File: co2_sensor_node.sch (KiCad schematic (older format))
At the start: 0 parts

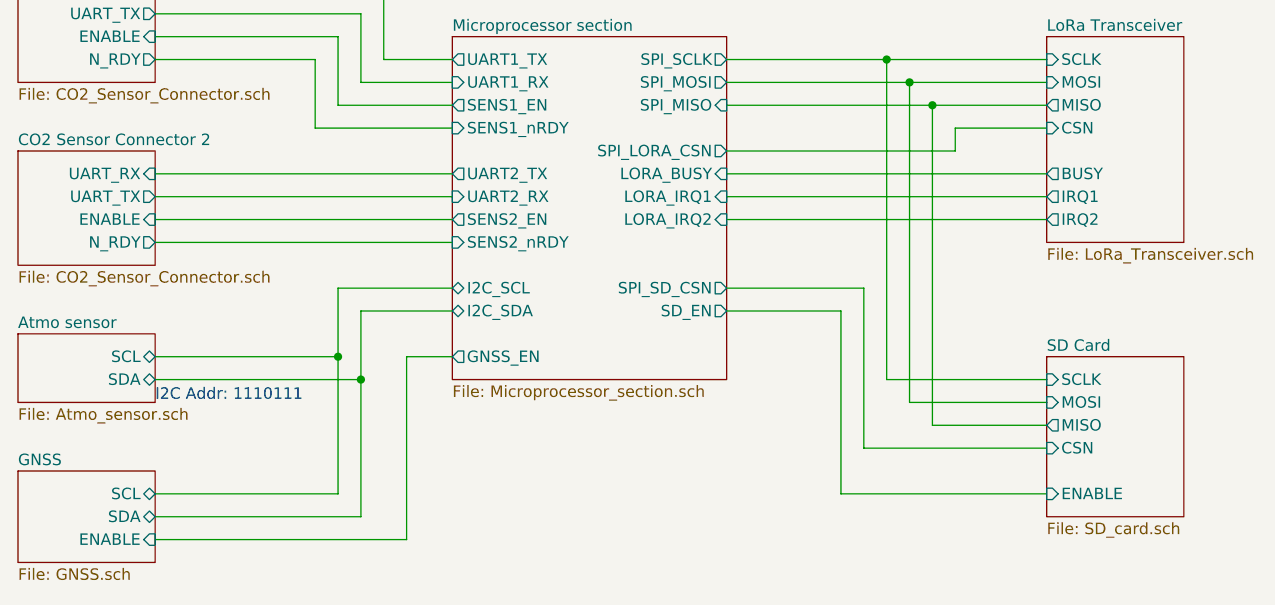
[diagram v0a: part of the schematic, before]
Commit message: Change BME280 out for connector
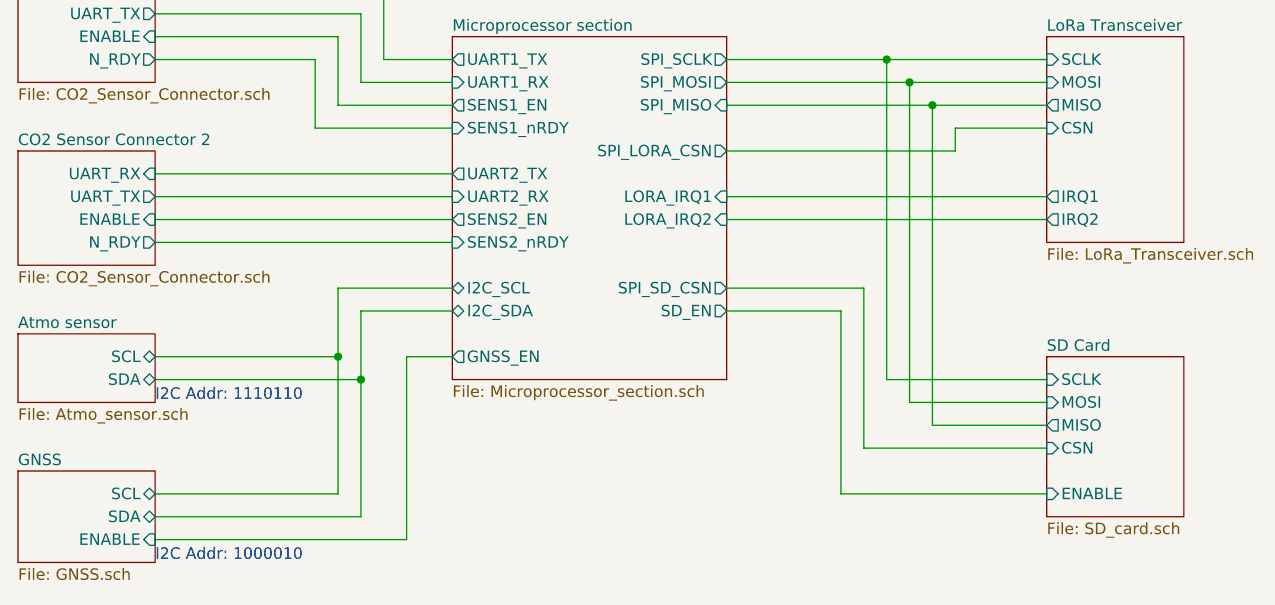
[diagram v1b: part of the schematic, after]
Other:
- note added: "I2C Addr: 1000010"
- note added: "I2C Addr: 1110110"
- note removed: "I2C Addr: 1110111"
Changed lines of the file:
@@
 F4 "MISO" O L 7500 3300 50
 F5 "CSN" I L 7500 3400 50
-F6 "BUSY" O L 7500 3600 50
-F7 "IRQ1" O L 7500 3700 50
-F8 "IRQ2" O L 7500 3800 50
+F6 "IRQ1" O L 7500 3700 50
+F7 "IRQ2" O L 7500 3800 50
 $EndSheet
 Wire Wire Line
@@
 	6800 4500 7500 4500
 Wire Wire Line
-	6100 3600 7500 3600
-Wire Wire Line
 	6100 3700 7500 3700
 Wire Wire Line
@@
 F15 "SENS2_EN" O L 4900 3800 50
 F16 "SENS2_nRDY" I L 4900 3900 50
-F17 "LORA_BUSY" I R 6100 3600 50
-F18 "LORA_IRQ1" I R 6100 3700 50
-F19 "LORA_IRQ2" I R 6100 3800 50
-F20 "GNSS_EN" O L 4900 4400 50
-F21 "SD_EN" O R 6100 4200 50
+F17 "LORA_IRQ1" I R 6100 3700 50
+F18 "LORA_IRQ2" I R 6100 3800 50
+F19 "GNSS_EN" O L 4900 4400 50
+F20 "SD_EN" O R 6100 4200 50
 $EndSheet
 Wire Wire Line
@@
 Wire Wire Line
 	3600 3600 4900 3600
+Text Notes 3600 5300 0    50   ~ 0
+I2C Addr: 1000010
 Text Notes 3600 4600 0    50   ~ 0
-I2C Addr: 1110111
+I2C Addr: 1110110
 $EndSCHEMATC

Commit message: Start PCB layout
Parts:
- added H1, H2, H3, H4: MountingHole, MountingHole:MountingHole_3.2mm_M3, symbol Mechanical:MountingHole
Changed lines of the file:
@@
 Text Notes 3600 4600 0    50   ~ 0
 I2C Addr: 1110110
+$Comp
+L Mechanical:MountingHole H1
+U 1 1 60AFB8C6
+P 9500 5000
+F 0 "H1" H 9600 5046 50  0000 L CNN
+F 1 "MountingHole" H 9600 4955 50  0000 L CNN
+F 2 "MountingHole:MountingHole_3.2mm_M3" H 9500 5000 50  0001 C CNN
+F 3 "~" H 9500 5000 50  0001 C CNN
+	1    9500 5000
+	1    0    0    -1
+$EndComp
+$Comp
+L Mechanical:MountingHole H2
+U 1 1 60AFC708
+P 9500 5200
+F 0 "H2" H 9600 5246 50  0000 L CNN
+F 1 "MountingHole" H 9600 5155 50  0000 L CNN
+F 2 "MountingHole:MountingHole_3.2mm_M3" H 9500 5200 50  0001 C CNN
+F 3 "~" H 9500 5200 50  0001 C CNN
+	1    9500 5200
+	1    0    0    -1
+$EndComp
+$Comp
+L Mechanical:MountingHole H3
+U 1 1 60AFC7FA
+P 9500 5400
+F 0 "H3" H 9600 5446 50  0000 L CNN
+F 1 "MountingHole" H 9600 5355 50  0000 L CNN
+F 2 "MountingHole:MountingHole_3.2mm_M3" H 9500 5400 50  0001 C CNN
+F 3 "~" H 9500 5400 50  0001 C CNN
+	1    9500 5400
+	1    0    0    -1
+$EndComp
+$Comp
+L Mechanical:MountingHole H4
+U 1 1 60AFC8FD
+P 9500 5600
+F 0 "H4" H 9600 5646 50  0000 L CNN
+F 1 "MountingHole" H 9600 5555 50  0000 L CNN
+F 2 "MountingHole:MountingHole_3.2mm_M3" H 9500 5600 50  0001 C CNN
+F 3 "~" H 9500 5600 50  0001 C CNN
+	1    9500 5600
+	1    0    0    -1
+$EndComp
 $EndSCHEMATC

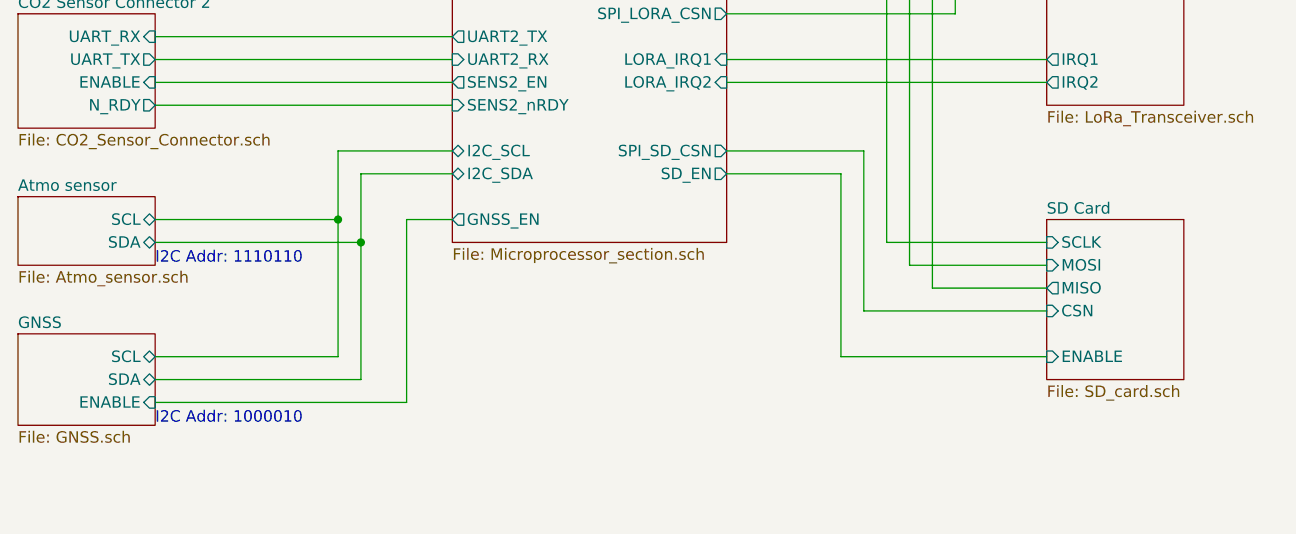
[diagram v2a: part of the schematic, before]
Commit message: Start changing design for long term chambers
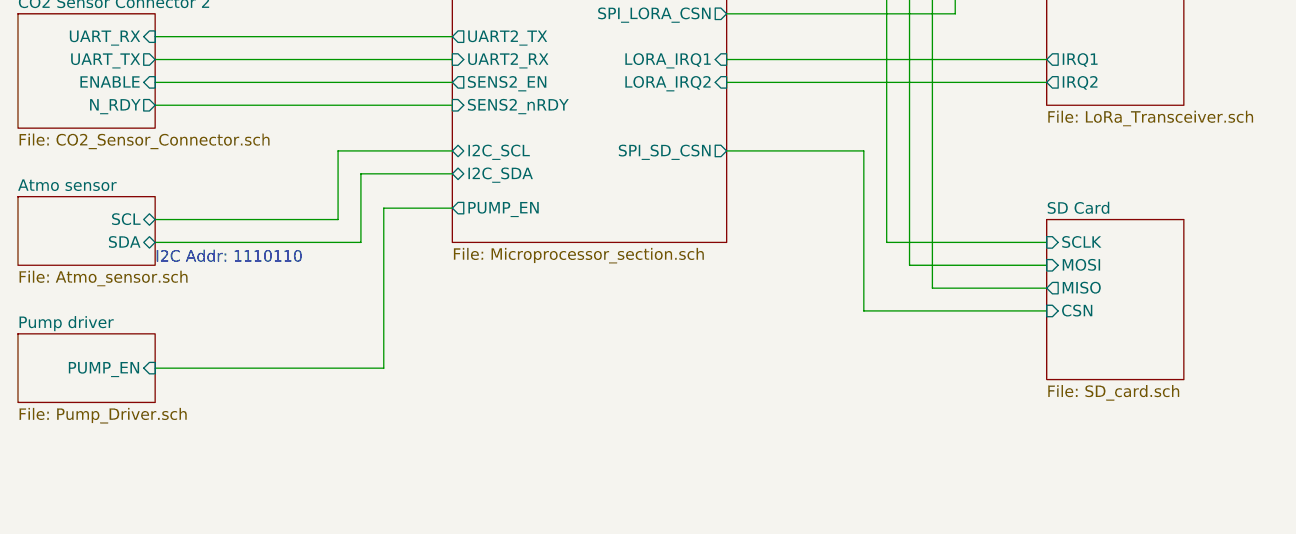
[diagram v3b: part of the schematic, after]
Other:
- note removed: "I2C Addr: 1000010"
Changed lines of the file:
@@
 F4 "MISO" O L 7500 4700 50
 F5 "CSN" I L 7500 4800 50
-F6 "ENABLE" I L 7500 5000 50
 $EndSheet
 $Sheet
@@
 	6100 3300 7000 3300
 Connection ~ 7000 3300
-$Sheet
-S 3000 4900 600  400
-U 60A8B3C8
-F0 "GNSS" 50
-F1 "GNSS.sch" 50
-F2 "SCL" B R 3600 5000 50
-F3 "SDA" B R 3600 5100 50
-F4 "ENABLE" I R 3600 5200 50
-$EndSheet
-Wire Wire Line
-	4400 4400 4400 5000
-Wire Wire Line
-	4400 5000 3600 5000
-Connection ~ 4400 4400
-Wire Wire Line
-	4500 4500 4500 5100
-Wire Wire Line
-	4500 5100 3600 5100
-Connection ~ 4500 4500
-Wire Wire Line
-	4900 4400 4700 4400
-Wire Wire Line
-	4700 4400 4700 5200
-Wire Wire Line
-	4700 5200 3600 5200
 Wire Wire Line
 	7100 3400 7500 3400
@@
 Wire Wire Line
 	7000 3300 7500 3300
-Wire Wire Line
-	6100 4200 6600 4200
-Wire Wire Line
-	6600 4200 6600 5000
-Wire Wire Line
-	6600 5000 7500 5000
 $Sheet
 S 3000 1700 500  500
@@
 F17 "LORA_IRQ1" I R 6100 3700 50
 F18 "LORA_IRQ2" I R 6100 3800 50
-F19 "GNSS_EN" O L 4900 4400 50
-F20 "SD_EN" O R 6100 4200 50
+F19 "PUMP_EN" O L 4900 4350 50
 $EndSheet
 Wire Wire Line
@@
 Wire Wire Line
 	3600 3600 4900 3600
-Text Notes 3600 5300 0    50   ~ 0
-I2C Addr: 1000010
 Text Notes 3600 4600 0    50   ~ 0
 I2C Addr: 1110110
@@
 	1    0    0    -1
 $EndComp
+$Sheet
+S 3000 4900 600  300
+U 60BD38F8
+F0 "Pump driver" 50
+F1 "Pump_Driver.sch" 50
+F2 "PUMP_EN" I R 3600 5050 50
+$EndSheet
+Wire Wire Line
+	4900 4350 4600 4350
+Wire Wire Line
+	4600 5050 3600 5050
+Wire Wire Line
+	4600 4350 4600 5050
 $EndSCHEMATC

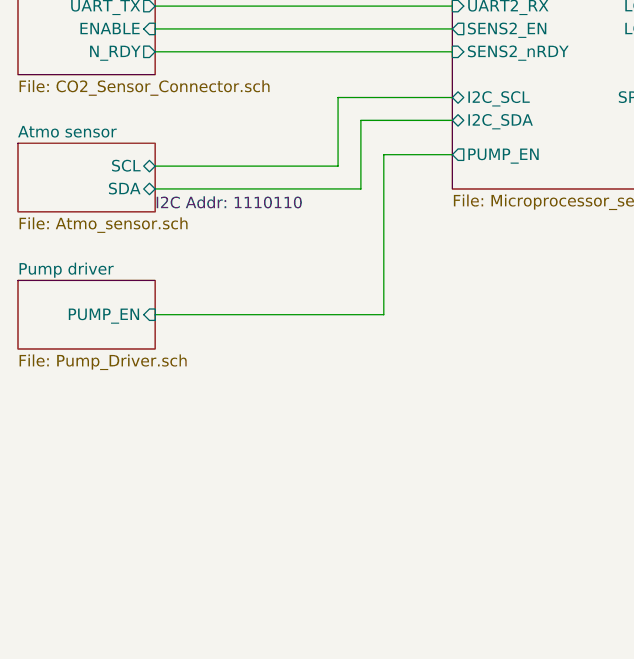
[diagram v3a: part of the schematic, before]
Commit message: Add connector for external chamber connection and change SMA to U.FL connector
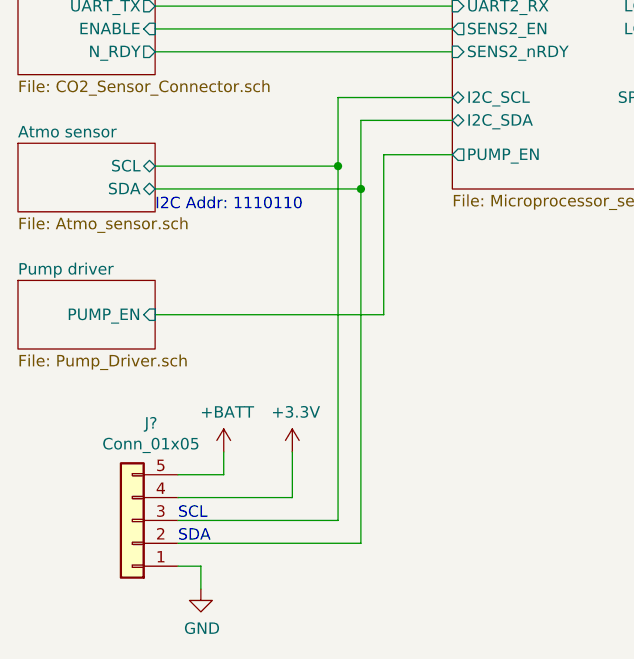
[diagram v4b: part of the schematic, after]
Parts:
- added J?: Conn_01x05, Connector_JST:JST_XH_B5B-XH-AM_1x05_P2.50mm_Vertical, symbol Connector_Generic:Conn_01x05
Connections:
- net Atmo sensor/SCL: now also J?.3 (Pin_3)
- net Atmo sensor/SDA: now also J?.2 (Pin_2)
- new net +3V3: J?.4 (Pin_4)
- new net +BATT: J?.5 (Pin_5)
- new net GND: J?.1 (Pin_1)
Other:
- note added: "SCL"
- note added: "SDA"
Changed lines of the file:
@@
 Wire Wire Line
 	4600 4350 4600 5050
+$Comp
+L Connector_Generic:Conn_01x05 J?
+U 1 1 6107D17A
+P 3500 5950
+F 0 "J?" H 3418 5525 50  0000 C CNN
+F 1 "Conn_01x05" H 3418 5616 50  0000 C CNN
+F 2 "Connector_JST:JST_XH_B5B-XH-AM_1x05_P2.50mm_Vertical" H 3418 5617 50  0001 C CNN
+F 3 "~" H 3500 5950 50  0001 C CNN
+	1    3500 5950
+	-1   0    0    1
+$EndComp
+$Comp
+L power:+BATT #PWR?
+U 1 1 6107E2E0
+P 3900 5650
+F 0 "#PWR?" H 3900 5500 50  0001 C CNN
+F 1 "+BATT" H 3915 5823 50  0000 C CNN
+F 2 "" H 3900 5650 50  0001 C CNN
+F 3 "" H 3900 5650 50  0001 C CNN
+	1    3900 5650
+	1    0    0    -1
+$EndComp
+$Comp
+L power:+3.3V #PWR?
+U 1 1 6107E8D3
+P 4200 5650
+F 0 "#PWR?" H 4200 5500 50  0001 C CNN
+F 1 "+3.3V" H 4215 5823 50  0000 C CNN
+F 2 "" H 4200 5650 50  0001 C CNN
+F 3 "" H 4200 5650 50  0001 C CNN
+	1    4200 5650
+	1    0    0    -1
+$EndComp
+$Comp
+L power:GND #PWR?
+U 1 1 6107ECD8
+P 3800 6250
+F 0 "#PWR?" H 3800 6000 50  0001 C CNN
+F 1 "GND" H 3805 6077 50  0000 C CNN
+F 2 "" H 3800 6250 50  0001 C CNN
+F 3 "" H 3800 6250 50  0001 C CNN
+	1    3800 6250
+	1    0    0    -1
+$EndComp
+Wire Wire Line
+	3700 6150 3800 6150
+Wire Wire Line
+	3800 6150 3800 6250
+Wire Wire Line
+	3700 5750 3900 5750
+Wire Wire Line
+	3900 5750 3900 5650
+Wire Wire Line
+	3700 5850 4200 5850
+Wire Wire Line
+	4200 5850 4200 5650
+Wire Wire Line
+	4400 4400 4400 5950
+Wire Wire Line
+	4400 5950 3700 5950
+Connection ~ 4400 4400
+Wire Wire Line
+	4500 4500 4500 6050
+Wire Wire Line
+	4500 6050 3700 6050
+Connection ~ 4500 4500
+Text Notes 3700 5950 0    50   ~ 0
+SCL
+Text Notes 3700 6050 0    50   ~ 0
+SDA
 $EndSCHEMATC

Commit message: Finalize schematic
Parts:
- removed J?: Conn_01x05, Connector_JST:JST_XH_B5B-XH-AM_1x05_P2.50mm_Vertical, symbol Connector_Generic:Conn_01x05
- added J?: Conn_01x04, Connector_JST:JST_XH_S4B-XH-A_1x04_P2.50mm_Horizontal, symbol Connector_Generic:Conn_01x04
- added J?: Conn_01x06, Connector_JST:JST_XH_S6B-XH-A_1x06_P2.50mm_Horizontal, symbol Connector_Generic:Conn_01x06
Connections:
- net +3V3: now also J?.1 (Pin_1), J?.2 (Pin_2)
- net +BATT: now also J?.1 (Pin_1)
- net Atmo sensor/SCL: now also J?.3 (Pin_3)
- net Atmo sensor/SDA: now also J?.4 (Pin_4)
- net GND: now also J?.3 (Pin_3), J?.4 (Pin_4), J?.5 (Pin_5), J?.6 (Pin_6)
- new net Microprocessor section/TEMPSENSOR: J?.2 (Pin_2)
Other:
- note added: "Header for\nexternal chamber"
- note added: "Temp header for use with DS18B20 sensor\n"
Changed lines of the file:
@@
 F18 "LORA_IRQ2" I R 6100 3800 50
 F19 "PUMP_EN" O L 4900 4350 50
+F20 "TEMPSENSOR" I R 6100 4350 50
 $EndSheet
 Wire Wire Line
@@
 	4600 4350 4600 5050
 $Comp
-L Connector_Generic:Conn_01x05 J?
-U 1 1 6107D17A
-P 3500 5950
-F 0 "J?" H 3418 5525 50  0000 C CNN
-F 1 "Conn_01x05" H 3418 5616 50  0000 C CNN
-F 2 "Connector_JST:JST_XH_B5B-XH-AM_1x05_P2.50mm_Vertical" H 3418 5617 50  0001 C CNN
-F 3 "~" H 3500 5950 50  0001 C CNN
-	1    3500 5950
-	-1   0    0    1
-$EndComp
-$Comp
-L power:+BATT #PWR?
+L power:+BATT #PWR08
 U 1 1 6107E2E0
 P 3900 5650
-F 0 "#PWR?" H 3900 5500 50  0001 C CNN
+F 0 "#PWR08" H 3900 5500 50  0001 C CNN
 F 1 "+BATT" H 3915 5823 50  0000 C CNN
 F 2 "" H 3900 5650 50  0001 C CNN
@@
 $EndComp
 $Comp
-L power:+3.3V #PWR?
+L power:+3.3V #PWR042
 U 1 1 6107E8D3
 P 4200 5650
-F 0 "#PWR?" H 4200 5500 50  0001 C CNN
+F 0 "#PWR042" H 4200 5500 50  0001 C CNN
 F 1 "+3.3V" H 4215 5823 50  0000 C CNN
 F 2 "" H 4200 5650 50  0001 C CNN
@@
 $EndComp
 $Comp
-L power:GND #PWR?
+L power:GND #PWR03
 U 1 1 6107ECD8
-P 3800 6250
-F 0 "#PWR?" H 3800 6000 50  0001 C CNN
-F 1 "GND" H 3805 6077 50  0000 C CNN
-F 2 "" H 3800 6250 50  0001 C CNN
-F 3 "" H 3800 6250 50  0001 C CNN
-	1    3800 6250
+P 3800 6350
+F 0 "#PWR03" H 3800 6100 50  0001 C CNN
+F 1 "GND" H 3805 6177 50  0000 C CNN
+F 2 "" H 3800 6350 50  0001 C CNN
+F 3 "" H 3800 6350 50  0001 C CNN
+	1    3800 6350
 	1    0    0    -1
 $EndComp
@@
 Wire Wire Line
 	4400 5950 3700 5950
-Connection ~ 4400 4400
 Wire Wire Line
 	4500 4500 4500 6050
 Wire Wire Line
 	4500 6050 3700 6050
-Connection ~ 4500 4500
 Text Notes 3700 5950 0    50   ~ 0
 SCL
 Text Notes 3700 6050 0    50   ~ 0
 SDA
+Connection ~ 4400 4400
+Connection ~ 4500 4500
+$Comp
+L power:+3.3V #PWR043
+U 1 1 60D3DB8F
+P 6500 5150
+F 0 "#PWR043" H 6500 5000 50  0001 C CNN
+F 1 "+3.3V" H 6515 5323 50  0000 C CNN
+F 2 "" H 6500 5150 50  0001 C CNN
+F 3 "" H 6500 5150 50  0001 C CNN
+	1    6500 5150
+	1    0    0    -1
+$EndComp
+$Comp
+L power:GND #PWR044
+U 1 1 60D3E07D
+P 6500 5600
+F 0 "#PWR044" H 6500 5350 50  0001 C CNN
+F 1 "GND" H 6505 5427 50  0000 C CNN
+F 2 "" H 6500 5600 50  0001 C CNN
+F 3 "" H 6500 5600 50  0001 C CNN
+	1    6500 5600
+	1    0    0    -1
+$EndComp
+Wire Wire Line
+	6500 5150 6500 5200
+Wire Wire Line
+	6500 5200 6600 5200
+Wire Wire Line
+	6500 5400 6600 5400
+Wire Wire Line
+	6100 4350 6250 4350
+Wire Wire Line
+	6250 4350 6250 5300
+Wire Wire Line
+	6250 5300 6600 5300
+$Comp
+L Connector_Generic:Conn_01x04 J?
+U 1 1 60D49B52
+P 6800 5300
+F 0 "J?" H 6880 5292 50  0000 L CNN
+F 1 "Conn_01x04" H 6880 5201 50  0000 L CNN
+F 2 "Connector_JST:JST_XH_S4B-XH-A_1x04_P2.50mm_Horizontal" H 6800 5300 50  0001 C CNN
+F 3 "~" H 6800 5300 50  0001 C CNN
+	1    6800 5300
+	1    0    0    -1
+$EndComp
+Wire Wire Line
+	6500 5600 6500 5500
+Wire Wire Line
+	6500 5500 6600 5500
+Wire Wire Line
+	6500 5400 6500 5500
+Connection ~ 6500 5500
+Text Notes 6900 5550 0    50   ~ 0
+Temp header for use with DS18B20 sensor\n
+Text Notes 2900 6450 0    50   ~ 0
+Header for\nexternal chamber
+$Comp
+L Connector_Generic:Conn_01x06 J?
+U 1 1 60D59C46
+P 3500 5950
+F 0 "J?" H 3418 6367 50  0000 C CNN
+F 1 "Conn_01x06" H 3418 6276 50  0000 C CNN
+F 2 "Connector_JST:JST_XH_S6B-XH-A_1x06_P2.50mm_Horizontal" H 3500 5950 50  0001 C CNN
+F 3 "~" H 3500 5950 50  0001 C CNN
+	1    3500 5950
+	-1   0    0    -1
+$EndComp
+Wire Wire Line
+	3700 6250 3800 6250
+Wire Wire Line
+	3800 6250 3800 6350
+Connection ~ 3800 6250
 $EndSCHEMATC
